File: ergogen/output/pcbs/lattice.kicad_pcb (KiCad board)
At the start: 2 copper layers, 114.3 x 81 mm, 69 parts

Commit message: 4 channel mux/demux
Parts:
- removed SW2, SW3: , SW_Slide_DPDT
- added C4: , 100n, B.Cu at (126.3, 69.2)
- added R7: , 10k, B.Cu at (159.4, 69.2)
- added U3: , USBLC6-2SC6, B.Cu at (114.3, 47.6)
- added U4: , USBLC6-2SC6, B.Cu at (171.4, 47.6)
- C3: footprint 100n -> 0.1uF
- R1: footprint 5k1 -> 10k
- R3: footprint 330R -> 5k1
- R4: footprint 10k -> 5k1
- R6: footprint 5k1 -> 330R
- SW1: footprint SW_Slide_DPDT -> SW_SPDT
- U2: footprint USBLC6-2SC6 -> TS3A44159PWR
- moved R6 59.3 mm to (126.3, 67.7), turned to 180 degrees
- moved R1 47.9 mm to (152.4, 51.7)
- moved R3 31.6 mm to (104.8, 44.6), turned to 0 degrees
- moved R4 31.6 mm to (181.0, 46.1)
- moved SW1 28.7 mm to (142.9, 45.0)
- moved C1 20.3 mm to (133.3, 50.2)
- moved C3 17.1 mm to (152.4, 50.2)
- moved C2 2.50 mm to (133.3, 51.7)
- moved U1 2.24 mm to (126.3, 47.6)
- moved U2 2.24 mm to (159.4, 47.6), turned to 0 degrees
- moved R2 1.50 mm to (104.8, 46.1)
- moved R5 1.50 mm to (181.0, 44.6)
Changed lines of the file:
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@@
+            )
+        )
+        (module CH552T (layer B.Cu)
+            (at 126.35 47.62500000000001 0)
+            (fp_text reference "U1" (at 0 0 0) (layer "B.Fab")
+              (effects (font (size 1 1) (thickness 0.15)))
+            )
+        )
+        (module 100n (layer B.Cu)
+            (at 133.35 50.150000000000006 0)
+            (fp_text reference "C1" (at 0 0 0) (layer "B.Fab")
+              (effects (font (size 1 1) (thickness 0.15)))
+            )
+        )
+        (module 100n (layer B.Cu)
+            (at 133.35 51.650000000000006 0)
+            (fp_text reference "C2" (at 0 0 0) (layer "B.Fab")
+              (effects (font (size 1 1) (thickness 0.15)))
+            )
+        )
+        (module TS3A44159PWR (layer B.Cu)
+            (at 159.4 47.62500000000001 0)
+            (fp_text reference "U2" (at 0 0 0) (layer "B.Fab")
+              (effects (font (size 1 1) (thickness 0.15)))
+            )
+        )
+        (module 0.1uF (layer B.Cu)
+            (at 152.4 50.150000000000006 0)
+            (fp_text reference "C3" (at 0 0 0) (layer "B.Fab")
+              (effects (font (size 1 1) (thickness 0.15)))
+            )
+        )
+        (module 10k (layer B.Cu)
+            (at 152.4 51.650000000000006 0)
+            (fp_text reference "R1" (at 0 0 0) (layer "B.Fab")
+              (effects (font (size 1 1) (thickness 0.15)))
+            )
+        )
+        (module SW_SPDT (layer B.Cu)
+            (at 142.875 44.95 0)
+            (fp_text reference "SW1" (at 0 0 0) (layer "B.Fab")
+              (effects (font (size 1 1) (thickness 0.15)))
             )
         )
@@
         (module 5k1 (layer B.Cu)
             (at 104.775 46.12500000000001 0)
-            (fp_text reference "R1" (at 0 0 0) (layer "B.Fab")
+            (fp_text reference "R2" (at 0 0 0) (layer "B.Fab")
               (effects (font (size 1 1) (thickness 0.15)))
             )
@@
         (module 5k1 (layer B.Cu)
             (at 104.775 44.62500000000001 0)
-            (fp_text reference "R2" (at 0 0 0) (layer "B.Fab")
-              (effects (font (size 1 1) (thickness 0.15)))
-            )
-        )
-        (module SW_Slide_DPDT (layer B.Cu)
-            (at 114.3 47.62500000000001 0)
-            (fp_text reference "SW1" (at 0 0 0) (layer "B.Fab")
-              (effects (font (size 1 1) (thickness 0.15)))
-            )
-        )
-        (module SW_Slide_DPDT (layer B.Cu)
-            (at 142.875 47.62500000000001 0)
-            (fp_text reference "SW2" (at 0 0 0) (layer "B.Fab")
-              (effects (font (size 1 1) (thickness 0.15)))
-            )
-        )
-        (module SW_Slide_DPDT (layer B.Cu)
-            (at 171.45 47.62500000000001 0)
-            (fp_text reference "SW3" (at 0 0 0) (layer "B.Fab")
-              (effects (font (size 1 1) (thickness 0.15)))
-            )
-        )
-        (module SW_SPST (layer B.Cu)
-            (at 133.35 69.2 0)
-            (fp_text reference "B1" (at 0 0 0) (layer "B.Fab")
-              (effects (font (size 1 1) (thickness 0.15)))
-            )
-        )
-        (module 330R (layer B.Cu)
-            (at 126.35 67.7 180)
             (fp_text reference "R3" (at 0 0 0) (layer "B.Fab")
               (effects (font (size 1 1) (thickness 0.15)))
             )
         )
-        (module 100n (layer B.Cu)
-            (at 126.35 69.2 0)
-            (fp_text reference "C1" (at 0 0 0) (layer "B.Fab")
-              (effects (font (size 1 1) (thickness 0.15)))
-            )
-        )
-        (module SW_SPST (layer B.Cu)
-            (at 152.4 69.2 0)
-            (fp_text reference "B2" (at 0 0 0) (layer "B.Fab")
-              (effects (font (size 1 1) (thickness 0.15)))
-            )
-        )
-        (module 10k (layer B.Cu)
-            (at 159.4 69.2 0)
-            (fp_text reference "R4" (at 0 0 0) (layer "B.Fab")
-              (effects (font (size 1 1) (thickness 0.15)))
-            )
-        )
-        (module CH552T (layer B.Cu)
-            (at 128.5875 47.62500000000001 0)
-            (fp_text reference "U1" (at 0 0 0) (layer "B.Fab")
-              (effects (font (size 1 1) (thickness 0.15)))
-            )
-        )
-        (module 100n (layer B.Cu)
-            (at 135.35 50.150000000000006 0)
-            (fp_text reference "C2" (at 0 0 0) (layer "B.Fab")
-              (effects (font (size 1 1) (thickness 0.15)))
-            )
-        )
-        (module 100n (layer B.Cu)
-            (at 135.35 51.650000000000006 0)
-            (fp_text reference "C3" (at 0 0 0) (layer "B.Fab")
-              (effects (font (size 1 1) (thickness 0.15)))
-            )
-        )
         (module USBLC6-2SC6 (layer B.Cu)
-            (at 157.1625 47.62500000000001 90)
-            (fp_text reference "U2" (at 0 0 0) (layer "B.Fab")
+            (at 114.3 47.62500000000001 0)
+            (fp_text reference "U3" (at 0 0 0) (layer "B.Fab")
               (effects (font (size 1 1) (thickness 0.15)))
             )
@@
         (module 5k1 (layer B.Cu)
             (at 180.975 46.12500000000001 0)
-            (fp_text reference "R5" (at 0 0 0) (layer "B.Fab")
+            (fp_text reference "R4" (at 0 0 0) (layer "B.Fab")
               (effects (font (size 1 1) (thickness 0.15)))
             )
@@
         (module 5k1 (layer B.Cu)
             (at 180.975 44.62500000000001 0)
+            (fp_text reference "R5" (at 0 0 0) (layer "B.Fab")
+              (effects (font (size 1 1) (thickness 0.15)))
+            )
+        )
+        (module USBLC6-2SC6 (layer B.Cu)
+            (at 171.45 47.62500000000001 0)
+            (fp_text reference "U4" (at 0 0 0) (layer "B.Fab")
+              (effects (font (size 1 1) (thickness 0.15)))
+            )
+        )
+        (module SW_SPST (layer B.Cu)
+            (at 133.35 69.2 0)
+            (fp_text reference "B1" (at 0 0 0) (layer "B.Fab")
+              (effects (font (size 1 1) (thickness 0.15)))
+            )
+        )
+        (module 330R (layer B.Cu)
+            (at 126.35 67.7 180)
             (fp_text reference "R6" (at 0 0 0) (layer "B.Fab")
               (effects (font (size 1 1) (thickness 0.15)))
             )
         )
-            (gr_text "lattice v2024.03" (at 180.975 66.675 0) (layer B.SilkS)
+        (module 100n (layer B.Cu)
+            (at 126.35 69.2 0)
+            (fp_text reference "C4" (at 0 0 0) (layer "B.Fab")
+              (effects (font (size 1 1) (thickness 0.15)))
+            )
+        )
+        (module SW_SPST (layer B.Cu)
+            (at 152.4 69.2 0)
+            (fp_text reference "B2" (at 0 0 0) (layer "B.Fab")
+              (effects (font (size 1 1) (thickness 0.15)))
+            )
+        )
+        (module 10k (layer B.Cu)
+            (at 159.4 69.2 0)
+            (fp_text reference "R7" (at 0 0 0) (layer "B.Fab")
+              (effects (font (size 1 1) (thickness 0.15)))
+            )
+        )
+            (gr_text "lattice v2024.03" (at 104.775 85.725 0) (layer B.SilkS)
                 (effects (font (size 1 1) (thickness 0.15)) (justify mirror))
             )

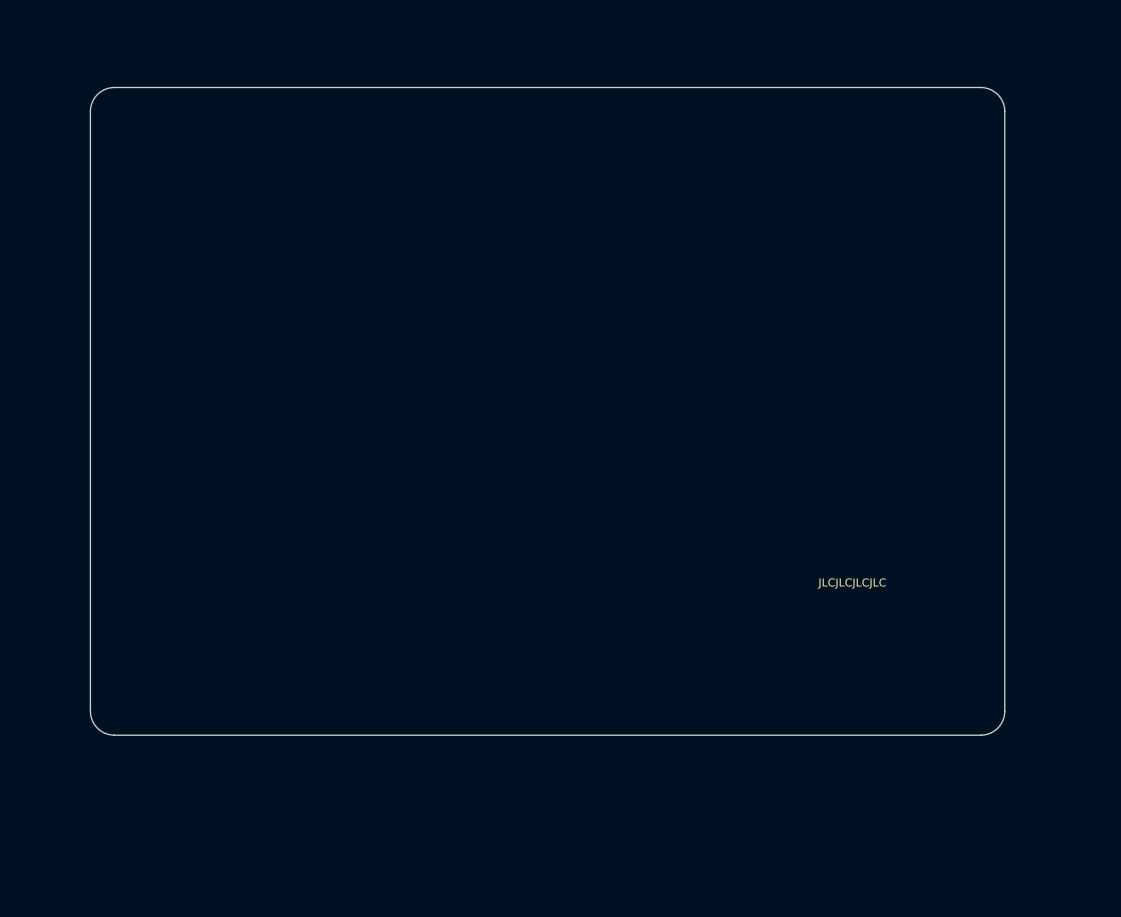
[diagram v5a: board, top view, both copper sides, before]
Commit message: CFX spacing, solder jumpers
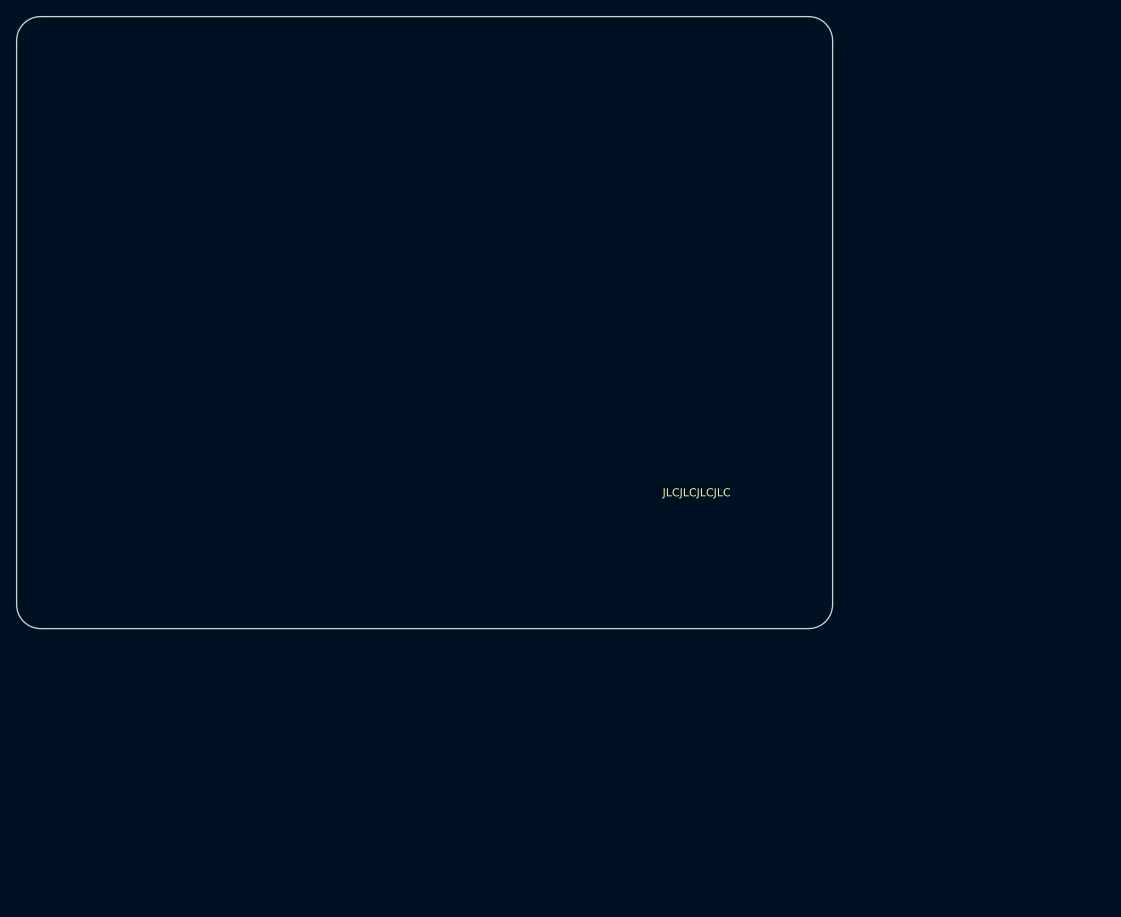
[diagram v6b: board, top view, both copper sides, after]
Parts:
- removed B2: , SW_SPST
- removed C3: , 0.1uF
- removed C4: , 100n
- removed MX1, MX10, MX11, MX12, MX13, MX14, MX15, MX16, MX17, MX18, MX19, MX2, MX20, MX21, MX22, MX23, MX24, MX3, MX4, MX5, MX6, MX7, MX8, MX9: , MX_SW_HS
- removed R6: , 330R
- removed R7: , 10k
- removed SW1: , SW_SPDT
- removed U4: , USBLC6-2SC6
- added JP1: , SolderJumper_3_Open, F.Cu at (106.0, 38.0)
- added JP2: , SolderJumper_3_Open, F.Cu at (108.5, 38.0)
- added JP3: , SolderJumper_3_Open, F.Cu at (111.0, 38.0)
- added JP4: , SolderJumper_3_Open, F.Cu at (113.5, 38.0)
- added JP5: , SolderJumper_3_Open, F.Cu at (116.0, 38.0)
- added JP6: , SolderJumper_3_Open, F.Cu at (118.5, 38.0)
- added K1: , SW_choc_v1_1u, F.Cu at (85.0, 102.0)
- added K10: , SW_choc_v1_1u, F.Cu at (119.0, 85.0)
- added K11: , SW_choc_v1_1u, F.Cu at (119.0, 68.0)
- added K12: , SW_choc_v1_1u, F.Cu at (119.0, 51.0)
- added K13: , SW_choc_v1_1u, F.Cu at (136.0, 102.0)
- added K14: , SW_choc_v1_1u, F.Cu at (136.0, 85.0)
- added K15: , SW_choc_v1_1u, F.Cu at (136.0, 68.0)
- added K16: , SW_choc_v1_1u, F.Cu at (136.0, 51.0)
- added K17: , SW_choc_v1_1u, F.Cu at (153.0, 102.0)
- added K18: , SW_choc_v1_1u, F.Cu at (153.0, 85.0)
- added K19: , SW_choc_v1_1u, F.Cu at (153.0, 68.0)
- added K2: , SW_choc_v1_1u, F.Cu at (85.0, 85.0)
- added K20: , SW_choc_v1_1u, F.Cu at (153.0, 51.0)
- added K21: , SW_choc_v1_1u, F.Cu at (170.0, 102.0)
- added K22: , SW_choc_v1_1u, F.Cu at (170.0, 85.0)
- added K23: , SW_choc_v1_1u, F.Cu at (170.0, 68.0)
- added K24: , SW_choc_v1_1u, F.Cu at (170.0, 51.0)
- added K3: , SW_choc_v1_1u, F.Cu at (85.0, 68.0)
- added K4: , SW_choc_v1_1u, F.Cu at (85.0, 51.0)
- added K5: , SW_choc_v1_1u, F.Cu at (102.0, 102.0)
- added K6: , SW_choc_v1_1u, F.Cu at (102.0, 85.0)
- added K7: , SW_choc_v1_1u, F.Cu at (102.0, 68.0)
- added K8: , SW_choc_v1_1u, F.Cu at (102.0, 51.0)
- added K9: , SW_choc_v1_1u, F.Cu at (119.0, 102.0)
- B1: footprint SW_SPST -> Pad_1x02; moved to F.Cu
- C1, C2, D1, D10, D11, D12, D13, D14, D15, D16, D17, D18, D19, D2, D20, D21, D22, D23, D24, D3, D4, D5, D6, D7, D8, D9, F1, F2, J1, J2, R2, R3, R4, U1, U3: moved to F.Cu
- R1: footprint 10k -> 5k1; moved to F.Cu
- R5: footprint 5k1 -> 10k; moved to F.Cu
- U2: footprint TS3A44159PWR -> USBLC6-2SC6; moved to F.Cu
- moved R1 60.5 mm to (93.5, 38.0)
- moved U2 60.2 mm to (100.0, 38.0)
- moved R3 57.1 mm to (161.5, 38.0)
- moved U3 41.8 mm to (155.0, 38.0)
- moved R5 33.1 mm to (148.5, 38.0), turned to 90 degrees
- moved B1 33.1 mm to (144.5, 38.0)
- moved F2 22.7 mm to (161.5, 36.0)
- moved J2 22.3 mm to (170.0, 36.2), turned to 180 degrees
- moved SYM1 21.5 mm to (161.5, 76.5)
- moved R4 20.4 mm to (161.5, 40.0)
- moved F1 16.2 mm to (93.5, 36.0)
- moved D21 14.4 mm to (170.0, 106.8), turned to 0 degrees
- moved C1 13.7 mm to (129.5, 37.0), turned to 180 degrees
- moved J1 13.5 mm to (85.0, 36.2), turned to 180 degrees
- moved D22 13.4 mm to (170.0, 89.8), turned to 0 degrees
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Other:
- board size 114.3 x 81 mm -> 102 x 76.5 mm
- board text added: "lattice v2025.01"
- board text removed: "lattice v2024.03"

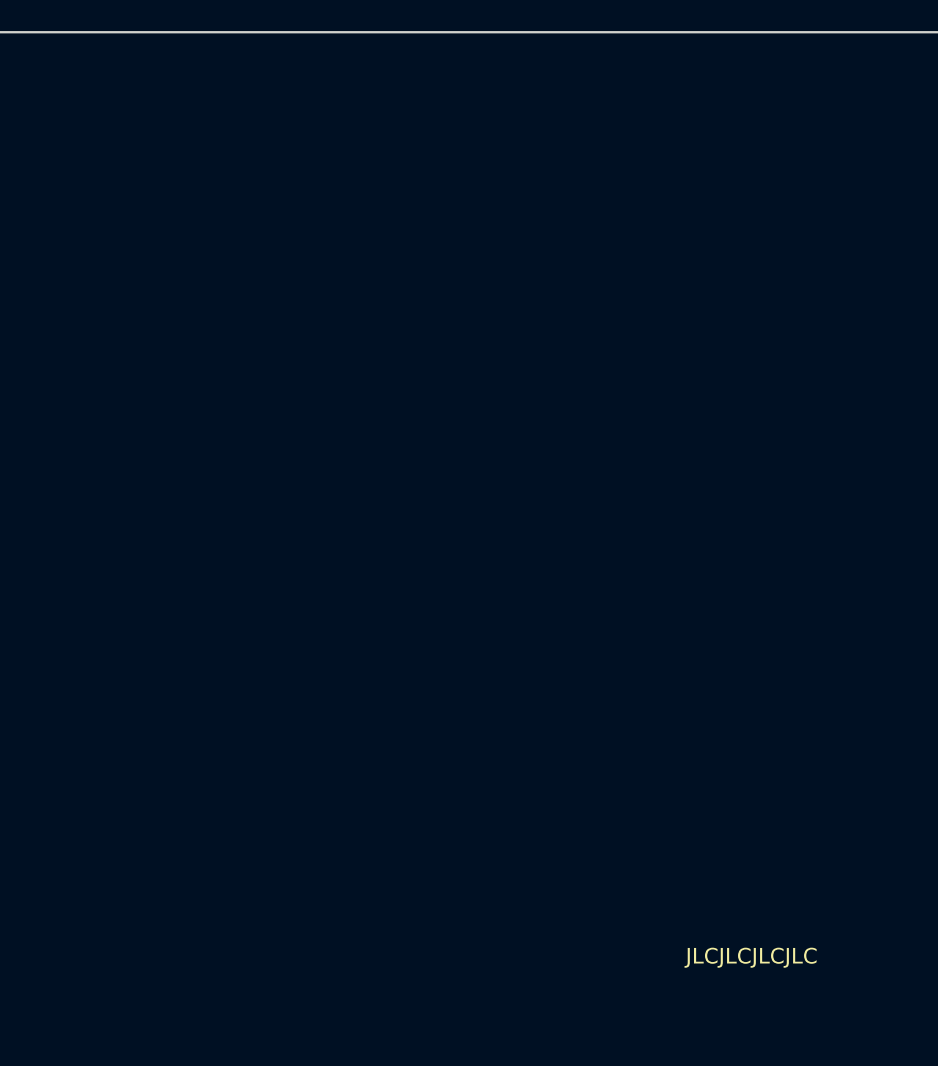
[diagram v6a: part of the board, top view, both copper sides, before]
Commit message: boot button, remove refereence designators, jumper labels
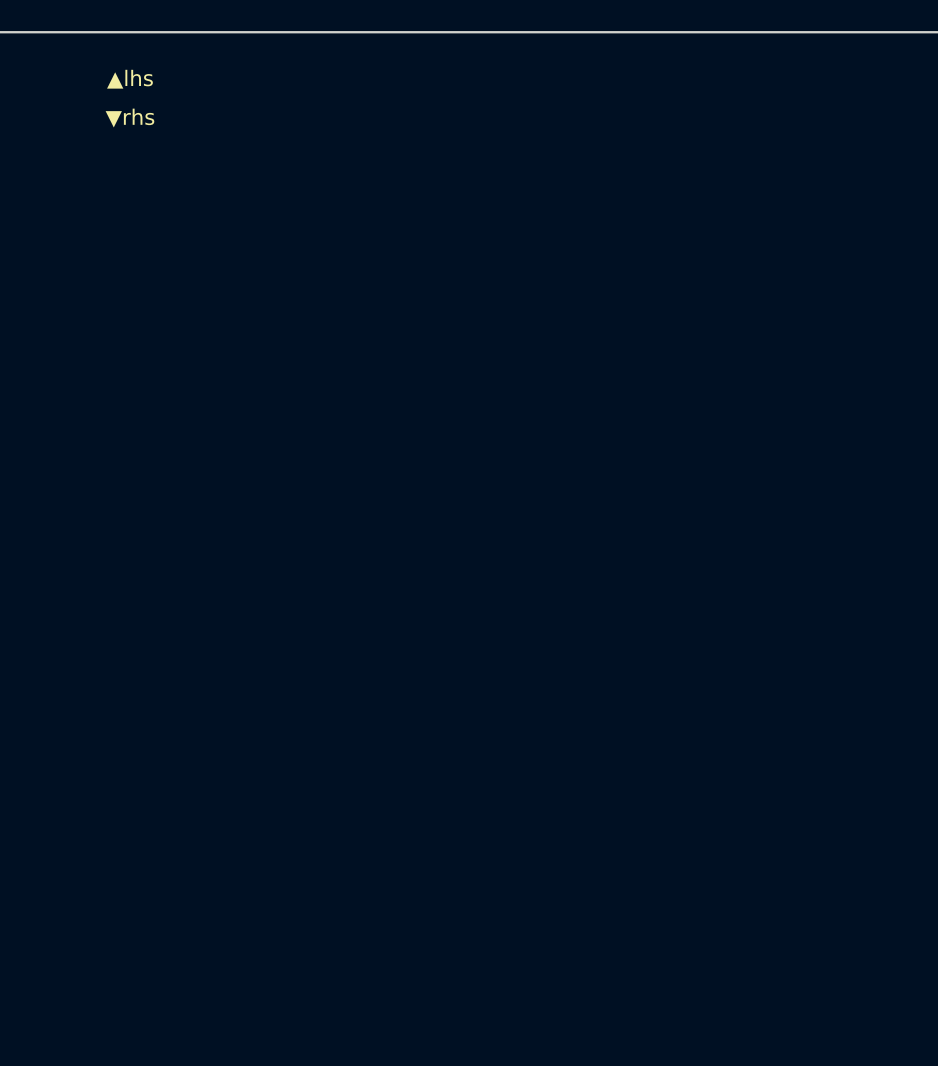
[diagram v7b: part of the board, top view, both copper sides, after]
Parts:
- B1: footprint Pad_1x02 -> SW_SPST_SKQG
- moved SYM1 17.0 mm to (161.5, 93.5)
- moved R5 12.7 mm to (136.0, 40.0), turned to 180 degrees
- moved D1 9.50 mm to (85.0, 97.2), turned to 180 degrees
- moved D10 9.50 mm to (119.0, 80.2), turned to 180 degrees
- moved D11 9.50 mm to (119.0, 63.2), turned to 180 degrees
- moved D12 9.50 mm to (119.0, 46.2), turned to 180 degrees
- moved D13 9.50 mm to (136.0, 97.2), turned to 180 degrees
- moved D14 9.50 mm to (136.0, 80.2), turned to 180 degrees
- moved D15 9.50 mm to (136.0, 63.2), turned to 180 degrees
- moved D16 9.50 mm to (136.0, 46.2), turned to 180 degrees
- moved D17 9.50 mm to (153.0, 97.2), turned to 180 degrees
- moved D18 9.50 mm to (153.0, 80.2), turned to 180 degrees
- moved D19 9.50 mm to (153.0, 63.2), turned to 180 degrees
- moved D2 9.50 mm to (85.0, 80.2), turned to 180 degrees
- moved D20 9.50 mm to (153.0, 46.2), turned to 180 degrees
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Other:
- board text added: "▲lhs"
- board text added: "▼rhs"
